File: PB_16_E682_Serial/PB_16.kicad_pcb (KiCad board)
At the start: 2 copper layers, 58 x 33 mm, 15 parts, among them J1 DMX1 RJ45, J2 DMX2 RJ45, J3 Serial In, SW1 DMX_Renard_Select, U1 UA9638CP

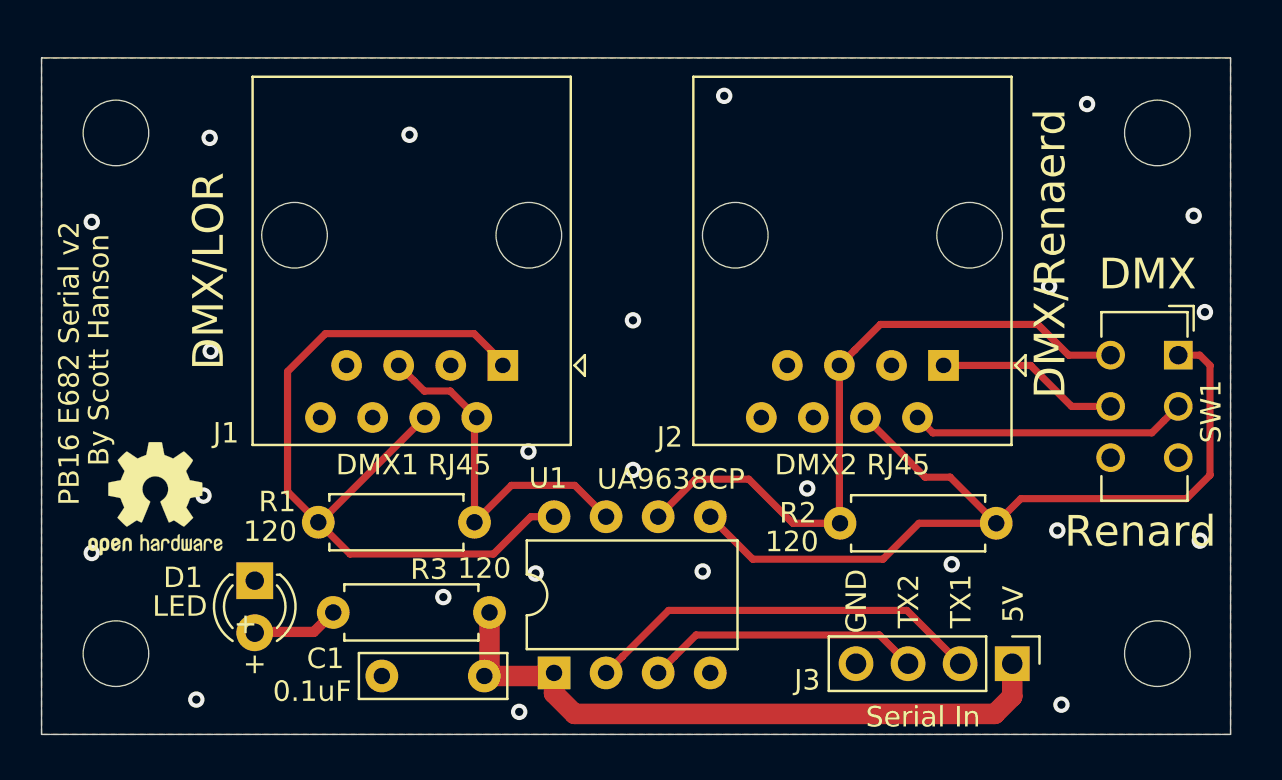
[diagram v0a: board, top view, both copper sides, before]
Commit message: redid serial connections
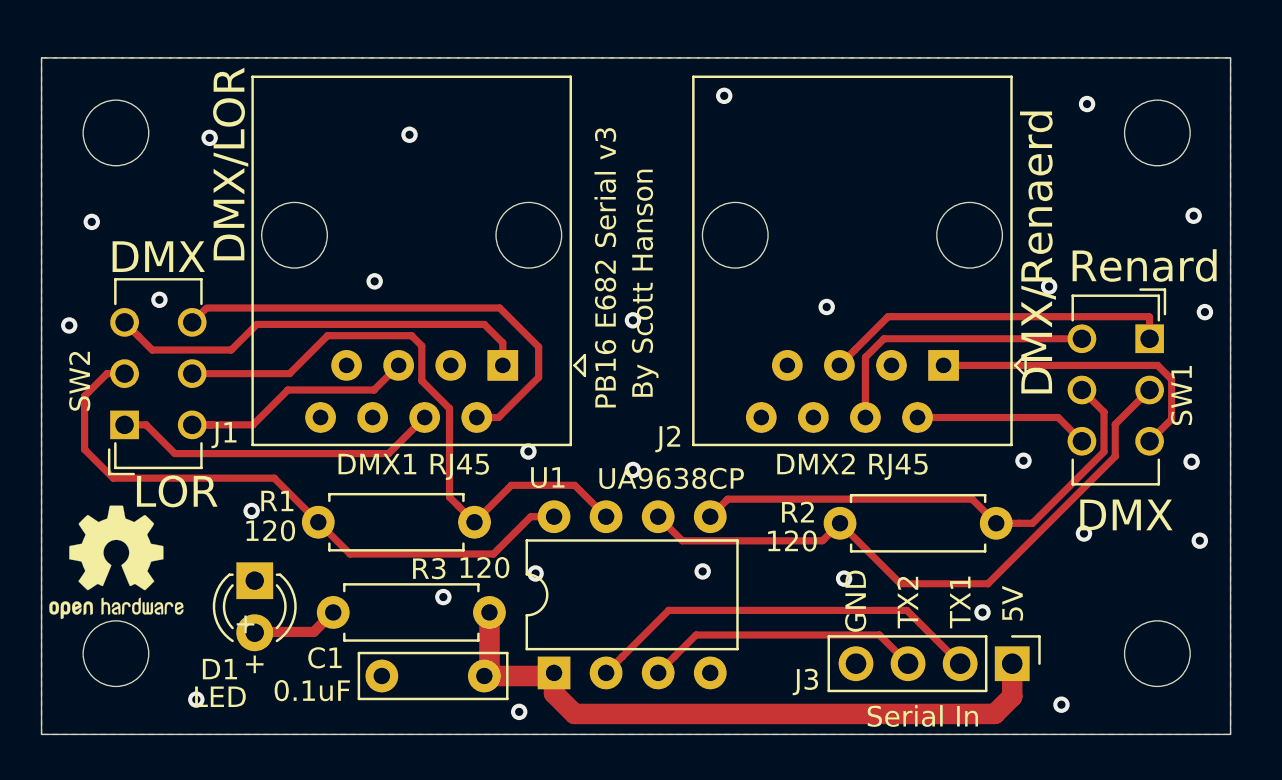
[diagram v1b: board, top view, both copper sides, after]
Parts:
- added SW2: DMX_LOR_Select, Button_Switch_THT:SW_CuK_JS202011CQN_DPDT_Straight, F.Cu at (88.0, 87.9)
- moved REF** 3.64 mm to (87.7, 94.6)
- moved SW1 1.61 mm to (138.1, 83.7)
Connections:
- J1 pad 1: /DMX1+ -> Net-(J1-Pad1)
- J1 pad 2: /DMX1- -> Net-(J1-Pad2)
- J1 pad 4: /DMX1+ -> Net-(J1-Pad4)
- J1 pad 5: /DMX1- -> Net-(J1-Pad5)
- J2 pad 4: /DMX2- -> Net-(J2-Pad4)
- J2 pad 5: /DMX2+ -> Net-(J2-Pad5)
- SW1 pad 1: /DMX2- -> Net-(J2-Pad5)
- SW1 pad 2: /Pin2 -> /DMX2+
- SW1 pad 3: GND -> /Pin1
- SW1 pad 4: /DMX2+ -> Net-(J2-Pad4)
- SW1 pad 5: /Pin1 -> /DMX2-
- SW1 pad 6: GND -> /Pin2
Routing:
- net Net-(J1-Pad2): track 0.00 -> 23.3 mm
- net Net-(J1-Pad1): track 0.00 -> 21.0 mm
- net /DMX2-: track 42.6 -> 25.0 mm
- net Net-(J2-Pad5): track 0.00 -> 17.2 mm
- net Net-(J1-Pad4): track 0.00 -> 15.9 mm
- net Net-(J2-Pad4): track 0.00 -> 13.9 mm
- net /DMX1-: track 17.8 -> 30.1 mm
- net Net-(J1-Pad5): track 0.00 -> 11.8 mm
- net /DMX1+: track 40.2 -> 30.9 mm
- net /Pin1: track 8.98 -> 14.9 mm
- net /Pin2: track 13.6 -> 8.50 mm
- net /DMX2+: track 32.9 -> 30.9 mm
- net GND: vias 24 -> 29
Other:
- board text added: "LOR"
- board text added: "PB16 E682 Serial v3"
- board text removed: "PB16 E682 Serial v2"

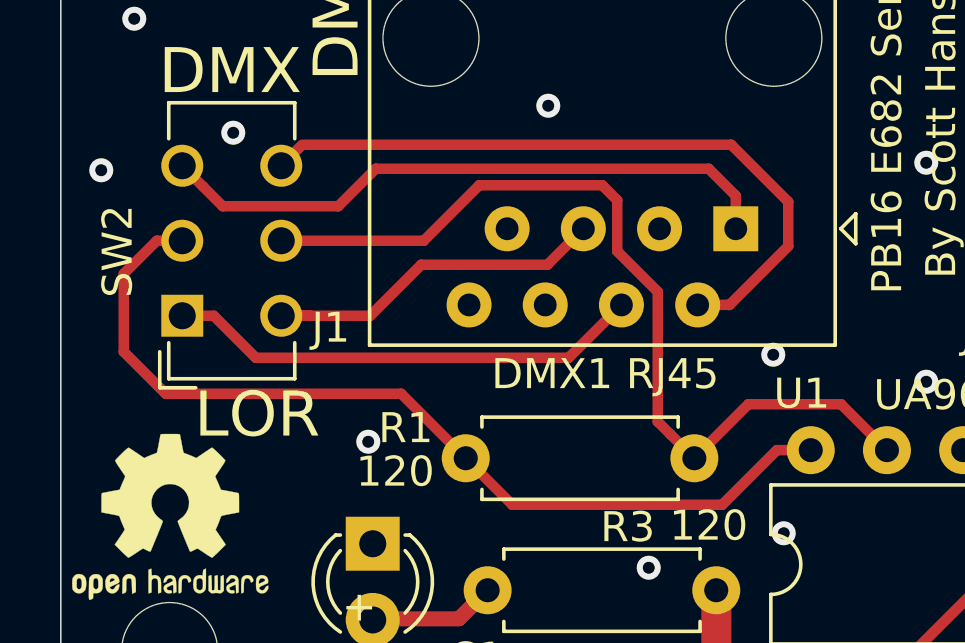
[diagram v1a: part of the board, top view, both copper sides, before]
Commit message: moved one trace and Updated PCB
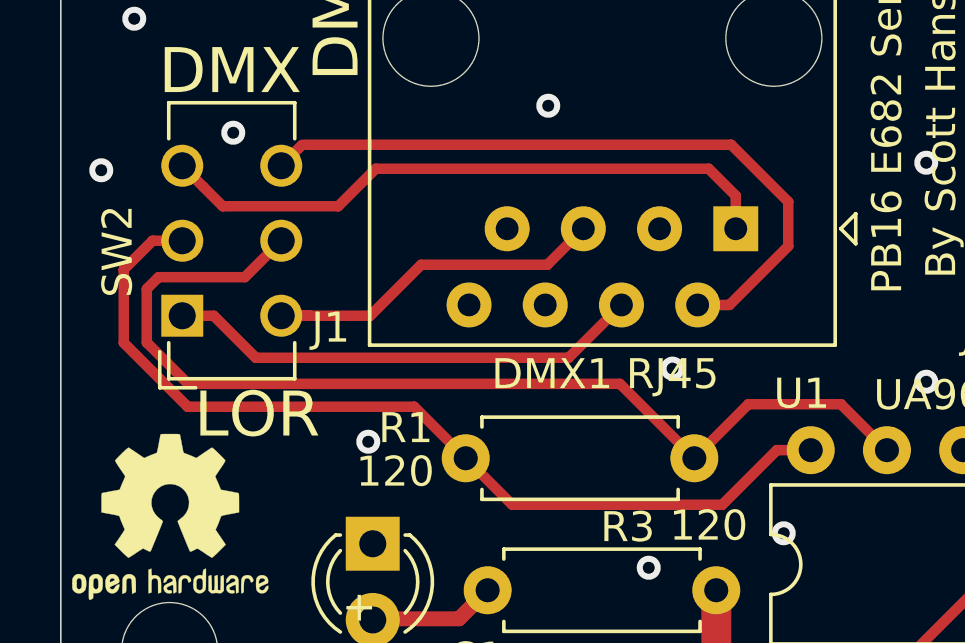
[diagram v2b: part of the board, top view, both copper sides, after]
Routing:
- net /DMX1-: track 30.1 -> 34.6 mm
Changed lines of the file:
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@@
-(kicad_pcb (version 20171130) (host pcbnew "(5.1.4)-1")
+(kicad_pcb (version 20171130) (host pcbnew "(5.1.5)-3")
   (general
     (thickness 1.6)
     (drawings 21)
-    (tracks 131)
+    (tracks 129)
     (zones 0)
     (modules 16)
@@
   (via (at 116.25 95.05) (size 0.8) (drill 0.4) (layers F.Cu B.Cu) (net 1))
   (via (at 108.1 95.15) (size 0.8) (drill 0.4) (layers F.Cu B.Cu) (net 1))
-  (via (at 107.75 89.2) (size 0.8) (drill 0.4) (layers F.Cu B.Cu) (net 1))
+  (via (at 104.394 89.662) (size 0.8) (drill 0.4) (layers F.Cu B.Cu) (net 1))
   (via (at 140.75 82.4) (size 0.8) (drill 0.4) (layers F.Cu B.Cu) (net 1))
   (via (at 140.2 77.7) (size 0.8) (drill 0.4) (layers F.Cu B.Cu) (net 1))
@@
   (segment (start 131.35 99.55) (end 131.35 101.15) (width 1) (layer F.Cu) (net 2))
   (segment (start 131.35 101.15) (end 130.5 102) (width 1) (layer F.Cu) (net 2))
-  (segment (start 105.12 87.65) (end 105.23 87.54) (width 0.35) (layer F.Cu) (net 17))
   (segment (start 111.54 92.38) (end 110.01 90.85) (width 0.35) (layer F.Cu) (net 3))
   (segment (start 106.92 90.85) (end 105.12 92.65) (width 0.35) (layer F.Cu) (net 3))
   (segment (start 110.01 90.85) (end 106.92 90.85) (width 0.35) (layer F.Cu) (net 3))
-  (segment (start 104.320001 91.850001) (end 105.12 92.65) (width 0.35) (layer F.Cu) (net 3))
-  (segment (start 103.9 91.43) (end 104.320001 91.850001) (width 0.35) (layer F.Cu) (net 3))
-  (segment (start 103.9 87.1) (end 103.9 91.43) (width 0.35) (layer F.Cu) (net 3))
-  (segment (start 90.85 85.4) (end 96.1 85.4) (width 0.35) (layer F.Cu) (net 3))
-  (segment (start 97.95 83.55) (end 102.05 83.55) (width 0.35) (layer F.Cu) (net 3))
-  (segment (start 96.1 85.4) (end 97.95 83.55) (width 0.35) (layer F.Cu) (net 3))
-  (segment (start 102.55 84.05) (end 102.55 85.75) (width 0.35) (layer F.Cu) (net 3))
-  (segment (start 102.05 83.55) (end 102.55 84.05) (width 0.35) (layer F.Cu) (net 3))
-  (segment (start 102.55 85.75) (end 103.9 87.1) (width 0.35) (layer F.Cu) (net 3))
+  (segment (start 102.64 90.17) (end 105.12 92.65) (width 0.35) (layer F.Cu) (net 3))
+  (segment (start 88.244998 90.17) (end 102.64 90.17) (width 0.35) (layer F.Cu) (net 3))
+  (segment (start 90.136 86.614) (end 87.260998 86.614) (width 0.35) (layer F.Cu) (net 3))
+  (segment (start 87.260998 86.614) (end 86.868 87.006998) (width 0.35) (layer F.Cu) (net 3))
+  (segment (start 91.35 85.4) (end 90.136 86.614) (width 0.35) (layer F.Cu) (net 3))
+  (segment (start 86.868 88.793002) (end 88.244998 90.17) (width 0.35) (layer F.Cu) (net 3))
+  (segment (start 86.868 87.006998) (end 86.868 88.793002) (width 0.35) (layer F.Cu) (net 3))
   (segment (start 97.5 92.65) (end 97.58 92.65) (width 0.35) (layer F.Cu) (net 4))
   (segment (start 107.86863 92.38) (end 106.04863 94.2) (width 0.35) (layer F.Cu) (net 4))
@@
   (segment (start 99.05 94.2) (end 97.5 92.65) (width 0.35) (layer F.Cu) (net 4))
   (segment (start 106.04863 94.2) (end 99.05 94.2) (width 0.35) (layer F.Cu) (net 4))
-  (segment (start 95.35 90.5) (end 97.5 92.65) (width 0.35) (layer F.Cu) (net 4))
-  (segment (start 87.5 90.5) (end 95.35 90.5) (width 0.35) (layer F.Cu) (net 4))
-  (segment (start 86.1 89.1) (end 87.5 90.5) (width 0.35) (layer F.Cu) (net 4))
-  (segment (start 86.1 86.5) (end 86.1 89.1) (width 0.35) (layer F.Cu) (net 4))
-  (segment (start 88.05 85.4) (end 87.2 85.4) (width 0.35) (layer F.Cu) (net 4))
-  (segment (start 87.2 85.4) (end 86.1 86.5) (width 0.35) (layer F.Cu) (net 4))
+  (segment (start 95.782 90.932) (end 97.5 92.65) (width 0.35) (layer F.Cu) (net 4))
+  (segment (start 87.060051 85.4) (end 86.1 86.360051) (width 0.35) (layer F.Cu) (net 4))
+  (segment (start 86.1 86.360051) (end 86.1 88.802835) (width 0.35) (layer F.Cu) (net 4))
+  (segment (start 88.05 85.4) (end 87.060051 85.4) (width 0.35) (layer F.Cu) (net 4))
+  (segment (start 86.1 88.802835) (end 88.229165 90.932) (width 0.35) (layer F.Cu) (net 4))
+  (segment (start 88.229165 90.932) (end 95.782 90.932) (width 0.35) (layer F.Cu) (net 4))
   (segment (start 122.92 92.67) (end 122.95 92.7) (width 0.35) (layer F.Cu) (net 7))
   (segment (start 136.375012 89.443823) (end 130.168835 95.65) (width 0.35) (layer F.Cu) (net 7))
@@
   (segment (start 100.93 89.3) (end 90.5 89.3) (width 0.35) (layer F.Cu) (net 16))
   (segment (start 102.69 87.54) (end 100.93 89.3) (width 0.35) (layer F.Cu) (net 16))
+  (segment (start 105.12 87.65) (end 105.23 87.54) (width 0.35) (layer F.Cu) (net 17))
   (segment (start 91.35 82.9) (end 92.049999 82.200001) (width 0.35) (layer F.Cu) (net 17))
   (segment (start 106.29066 87.54) (end 105.23 87.54) (width 0.35) (layer F.Cu) (net 17))
